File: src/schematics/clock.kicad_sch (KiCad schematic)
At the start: 2 parts, among them U7 XLH335040.000000I

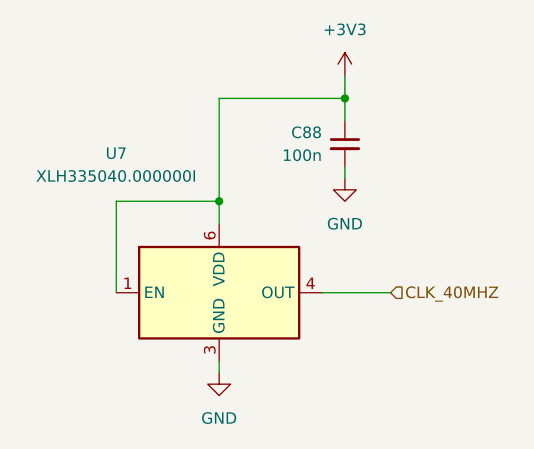
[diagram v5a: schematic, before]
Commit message: ✅ Check each IC's supply voltage in the schematic
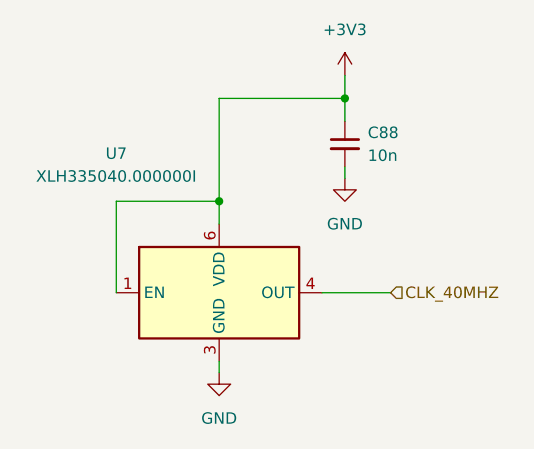
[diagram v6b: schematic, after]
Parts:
- C88: value 100n -> 10n
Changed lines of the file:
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@@
 		(fields_autoplaced yes)
 		(property "Reference" "C88"
-			(at 166.37 74.9362 0)
+			(at 171.45 74.9362 0)
 			(effects
 				(font
 					(size 1.27 1.27)
 				)
-				(justify left)
+				(justify right)
 			)
 		)
-		(property "Value" "100n"
-			(at 166.37 77.4762 0)
+		(property "Value" "10n"
+			(at 171.45 77.4762 0)
 			(effects
 				(font
 					(size 1.27 1.27)
 				)
-				(justify left)
+				(justify right)
 			)
 		)

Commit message: Add footprint for oscillator (#70)
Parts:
- U7: footprint (none) -> ECAP5-DPROC:XLH335040.000000I
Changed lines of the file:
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@@
 			)
 		)
-		(property "Footprint" ""
+		(property "Footprint" "ECAP5-DPROC:XLH335040.000000I"
 			(at 160.655 104.14 0)
 			(effects

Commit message: Add remaining component footprints (#79)
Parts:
- C88: footprint (none) -> Capacitor_SMD:C_0402_1005Metric
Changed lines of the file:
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@@
 			)
 		)
-		(property "Footprint" ""
+		(property "Footprint" "Capacitor_SMD:C_0402_1005Metric"
 			(at 168.91 76.2 0)
 			(effects
